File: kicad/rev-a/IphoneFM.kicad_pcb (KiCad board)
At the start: 2 copper layers, 0 parts

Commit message: Step 3.4: board outline at the sketch's coordinates, origins on its top-left corner
Co-Authored-By: Claude Opus 5.5 <noreply@anthropic.com>
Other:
- board outline added: 46.5 x 71.4 mm
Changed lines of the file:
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@@
 		(capping no)
 		(filling no)
+		(aux_axis_origin 12.7 59.56)
+		(grid_origin 12.7 59.56)
 		(pcbplotparams
 			(layerselection 0x00000000_00000000_55555555_5755f5ff)
@@
 		)
 	)
+	(gr_rect
+		(start 12.7 59.56)
+		(end 59.15 130.96)
+		(stroke
+			(width 0.05)
+			(type solid)
+		)
+		(fill no)
+		(layer "Edge.Cuts")
+	)
 	(embedded_fonts no)

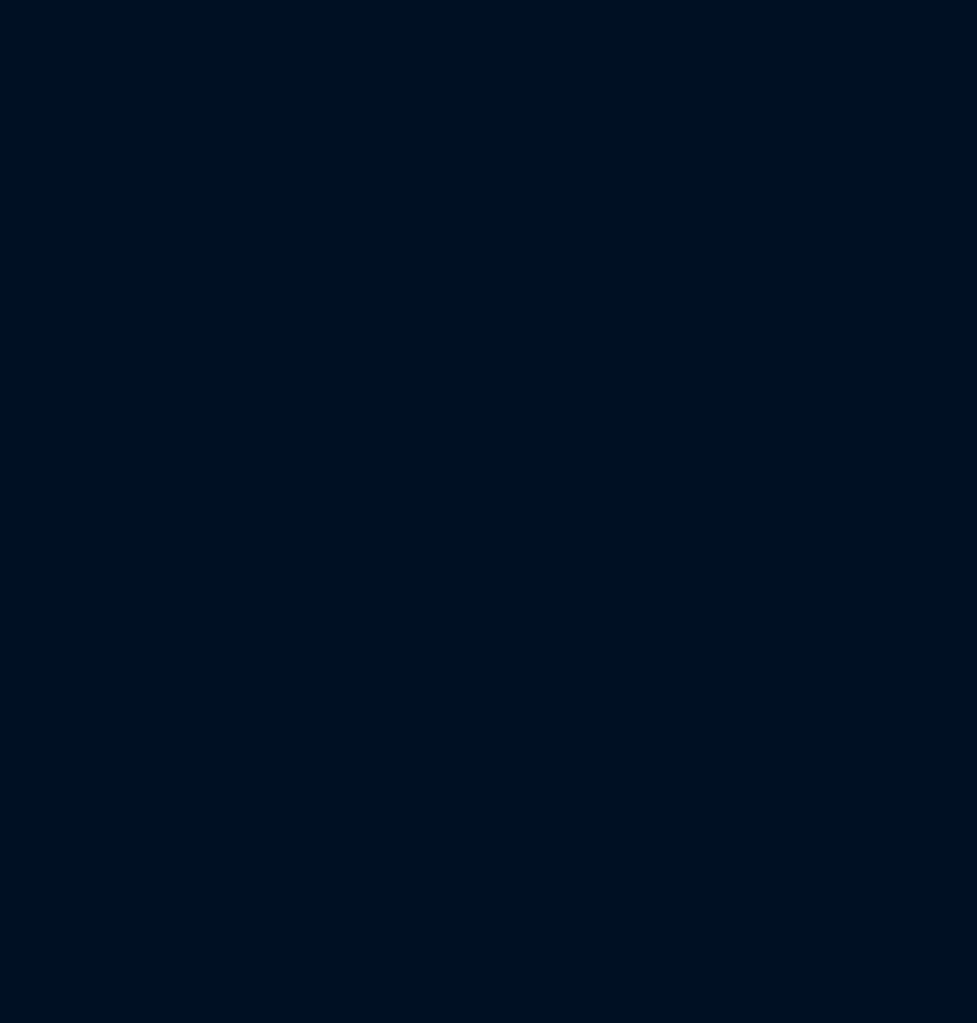
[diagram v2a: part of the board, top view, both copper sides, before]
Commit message: Step 4.1: parts brought across from the schematic (106 footprints), rules restored after KiCad's stale save, mask material named so KiCad keeps its Dk
Co-Authored-By: Claude Opus 5.5 <noreply@anthropic.com>
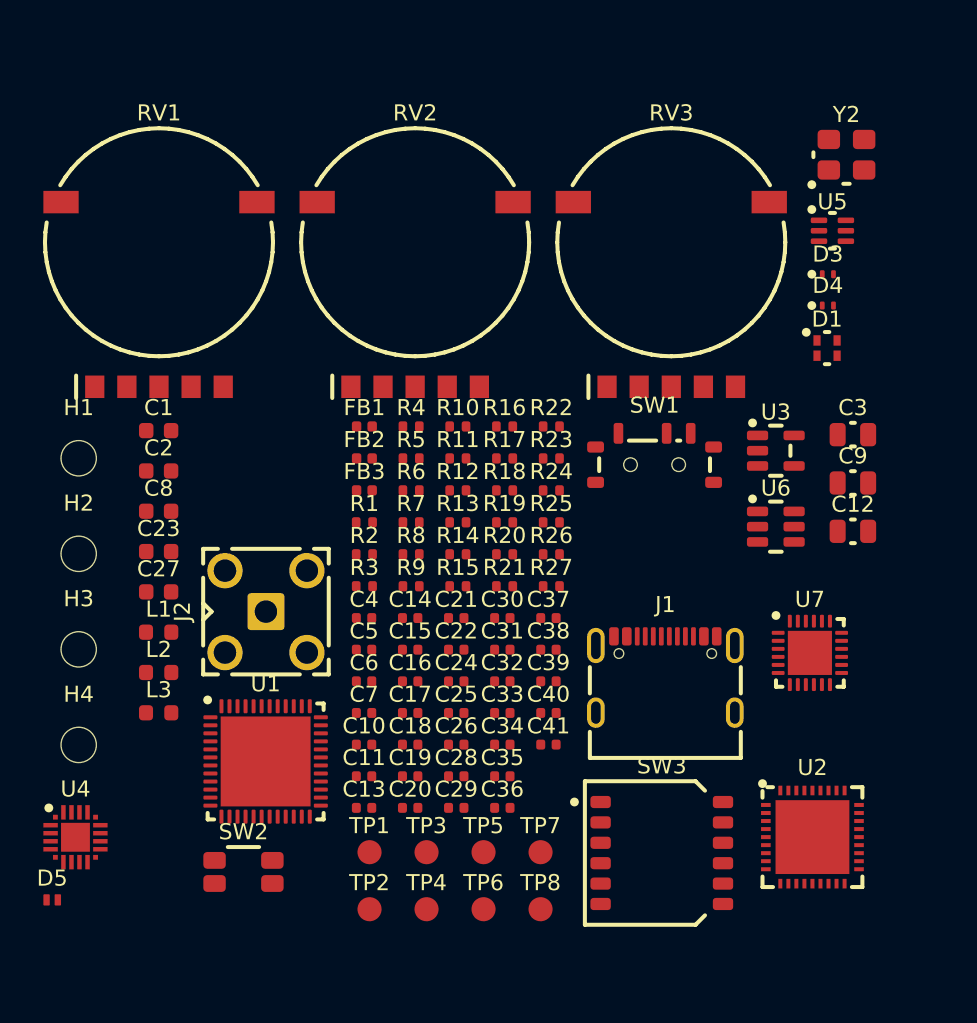
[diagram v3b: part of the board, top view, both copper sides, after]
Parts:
- added C1: 1 µF X7R 16 V, IphoneFM:C_0603_1608Metric, F.Cu at (-45.8, 85.1)
- added C10: 100 nF X7R 16 V, IphoneFM:C_0402_1005Metric, F.Cu at (-33.1, 104.6)
- added C11: 100 nF X7R 16 V, IphoneFM:C_0402_1005Metric, F.Cu at (-33.1, 106.6)
- added C12: 10 µF X5R 16 V, IphoneFM:C_0805_2012Metric, F.Cu at (-2.62, 91.3)
- added C13: 100 nF X7R 16 V, IphoneFM:C_0402_1005Metric, F.Cu at (-33.1, 108.6)
- added C14: 100 nF X7R 16 V, IphoneFM:C_0402_1005Metric, F.Cu at (-30.2, 96.7)
- added C15: 100 nF X7R 16 V, IphoneFM:C_0402_1005Metric, F.Cu at (-30.2, 98.7)
- added C16: 100 nF X7R 16 V, IphoneFM:C_0402_1005Metric, F.Cu at (-30.2, 100.7)
- added C17: 100 nF X7R 16 V, IphoneFM:C_0402_1005Metric, F.Cu at (-30.2, 102.6)
- added C18: 100 nF X7R 16 V, IphoneFM:C_0402_1005Metric, F.Cu at (-30.2, 104.6)
- added C19: 100 nF X7R 16 V, IphoneFM:C_0402_1005Metric, F.Cu at (-30.2, 106.6)
- added C2: 1 µF X7R 16 V, IphoneFM:C_0603_1608Metric, F.Cu at (-45.8, 87.6)
- added C20: 100 nF X7R 16 V, IphoneFM:C_0402_1005Metric, F.Cu at (-30.2, 108.6)
- added C21: 100 nF X7R 16 V, IphoneFM:C_0402_1005Metric, F.Cu at (-27.3, 96.7)
- added C22: 100 nF X7R 16 V, IphoneFM:C_0402_1005Metric, F.Cu at (-27.3, 98.7)
- added C23: 2.2 µF X5R 16 V, IphoneFM:C_0603_1608Metric, F.Cu at (-45.8, 92.6)
- added C24: 100 pF C0G, IphoneFM:C_0402_1005Metric, F.Cu at (-27.3, 100.7)
- added C25: 1.5 nF C0G, IphoneFM:C_0402_1005Metric, F.Cu at (-27.3, 102.6)
- added C26: 100 pF C0G, IphoneFM:C_0402_1005Metric, F.Cu at (-27.3, 104.6)
- added C27: 1 µF X7R 16 V, IphoneFM:C_0603_1608Metric, F.Cu at (-45.8, 95.1)
- added C28: 33 pF C0G, IphoneFM:C_0402_1005Metric, F.Cu at (-27.3, 106.6)
- added C29: 56 pF C0G, IphoneFM:C_0402_1005Metric, F.Cu at (-27.3, 108.6)
- added C3: 10 µF X5R 16 V, IphoneFM:C_0805_2012Metric, F.Cu at (-2.62, 85.3)
- added C30: 33 pF C0G, IphoneFM:C_0402_1005Metric, F.Cu at (-24.4, 96.7)
- added C31: 1 nF C0G, IphoneFM:C_0402_1005Metric, F.Cu at (-24.4, 98.7)
- added C32: 22 nF X7R 50 V, IphoneFM:C_0402_1005Metric, F.Cu at (-24.4, 100.7)
- added C33: 100 nF X7R 16 V, IphoneFM:C_0402_1005Metric, F.Cu at (-24.4, 102.6)
- added C34: 1 nF C0G, IphoneFM:C_0402_1005Metric, F.Cu at (-24.4, 104.6)
- added C35: 6 pF C0G, IphoneFM:C_0402_1005Metric, F.Cu at (-24.4, 106.6)
- added C36: 3.3 pF C0G, IphoneFM:C_0402_1005Metric, F.Cu at (-24.4, 108.6)
- added C37: 33 pF C0G, IphoneFM:C_0402_1005Metric, F.Cu at (-21.6, 96.7)
- added C38: 33 pF C0G, IphoneFM:C_0402_1005Metric, F.Cu at (-21.6, 98.7)
- added C39: 100 nF X7R 16 V, IphoneFM:C_0402_1005Metric, F.Cu at (-21.6, 100.7)
- added C4: 100 nF X7R 16 V, IphoneFM:C_0402_1005Metric, F.Cu at (-33.1, 96.7)
- added C40: 100 nF X7R 16 V, IphoneFM:C_0402_1005Metric, F.Cu at (-21.6, 102.6)
- added C41: 100 nF X7R 16 V, IphoneFM:C_0402_1005Metric, F.Cu at (-21.6, 104.6)
- added C5: 100 nF X7R 16 V, IphoneFM:C_0402_1005Metric, F.Cu at (-33.1, 98.7)
- added C6: 100 nF X7R 16 V, IphoneFM:C_0402_1005Metric, F.Cu at (-33.1, 100.7)
- added C7: 100 nF X7R 16 V, IphoneFM:C_0402_1005Metric, F.Cu at (-33.1, 102.6)
- added C8: 1 µF X7R 16 V, IphoneFM:C_0603_1608Metric, F.Cu at (-45.8, 90.1)
- added C9: 4.7 µF X7R 16 V, IphoneFM:C_0805_2012Metric, F.Cu at (-2.62, 88.3)
- added D1: RGB LED, common anode, IphoneFM:LED_RGB_XINGLIGHT_XL-1615RGBC_1.6x1.5mm, F.Cu at (-4.22, 79.9)
- added D3: ESD 5.5 V, IphoneFM:Texas_DPY0002A_0.6x1mm_P0.65mm, F.Cu at (-4.17, 75.3)
- added D4: ESD 5.5 V, IphoneFM:Texas_DPY0002A_0.6x1mm_P0.65mm, F.Cu at (-4.17, 77.3)
- added D5: ESD 5 V, 0.5 pF, IphoneFM:D_SOD-882, F.Cu at (-52.5, 114.3)
- added FB1: 75 Ω at 100 MHz, IphoneFM:L_0402_1005Metric, F.Cu at (-33.0, 84.8)
- added FB2: 600 Ω at 100 MHz, IphoneFM:L_0402_1005Metric, F.Cu at (-33.0, 86.8)
- added FB3: 600 Ω at 100 MHz, IphoneFM:L_0402_1005Metric, F.Cu at (-33.0, 88.8)
- added H1: M2, IphoneFM:MountingHole_2.2mm_M2, F.Cu at (-50.8, 86.8)
- added H2: M2, IphoneFM:MountingHole_2.2mm_M2, F.Cu at (-50.8, 92.7)
- added H3: M2, IphoneFM:MountingHole_2.2mm_M2, F.Cu at (-50.8, 98.7)
- added H4: M2, IphoneFM:MountingHole_2.2mm_M2, F.Cu at (-50.8, 104.6)
- added J1: USB 2.0 Type-C, IphoneFM:USB_C_Receptacle_HRO_TYPE-C-31-M-12_2020, F.Cu at (-14.3, 101.5)
- added J2: SMA jack, IphoneFM:SMA_BAT_Wireless_BWSMA-KWE-Z001, F.Cu at (-39.2, 96.3)
- added L1: 150 nH 2%, IphoneFM:L_0603_1608Metric, F.Cu at (-45.8, 97.6)
- added L2: 100 nH 2%, IphoneFM:L_0603_1608Metric, F.Cu at (-45.8, 100.1)
- added L3: 100 nH 2%, IphoneFM:L_0603_1608Metric, F.Cu at (-45.8, 102.6)
- added R1: 5.1 kΩ 1%, IphoneFM:R_0402_1005Metric, F.Cu at (-33.0, 90.8)
- added R10: 10 kΩ 1%, IphoneFM:R_0402_1005Metric, F.Cu at (-27.2, 84.8)
- added R11: 10 kΩ 1%, IphoneFM:R_0402_1005Metric, F.Cu at (-27.2, 86.8)
- added R12: 10 kΩ 1%, IphoneFM:R_0402_1005Metric, F.Cu at (-27.2, 88.8)
- added R13: 10 kΩ 1%, IphoneFM:R_0402_1005Metric, F.Cu at (-27.2, 90.8)
- added R14: 10 kΩ 1%, IphoneFM:R_0402_1005Metric, F.Cu at (-27.2, 92.8)
- added R15: 10 kΩ 1%, IphoneFM:R_0402_1005Metric, F.Cu at (-27.2, 94.8)
- added R16: 1 kΩ 1%, IphoneFM:R_0402_1005Metric, F.Cu at (-24.3, 84.8)
- added R17: 1 kΩ 1%, IphoneFM:R_0402_1005Metric, F.Cu at (-24.3, 86.8)
- added R18: 100 kΩ 1%, IphoneFM:R_0402_1005Metric, F.Cu at (-24.3, 88.8)
- added R19: 10 kΩ 1%, IphoneFM:R_0402_1005Metric, F.Cu at (-24.3, 90.8)
- added R2: 5.1 kΩ 1%, IphoneFM:R_0402_1005Metric, F.Cu at (-33.0, 92.8)
- added R20: 6.8 kΩ 1%, IphoneFM:R_0402_1005Metric, F.Cu at (-24.3, 92.8)
- added R21: 6.8 kΩ 1%, IphoneFM:R_0402_1005Metric, F.Cu at (-24.3, 94.8)
- added R22: 604 Ω 1%, IphoneFM:R_0402_1005Metric, F.Cu at (-21.4, 84.8)
- added R23: 2 kΩ 1%, IphoneFM:R_0402_1005Metric, F.Cu at (-21.4, 86.8)
- added R24: 2 kΩ 1%, IphoneFM:R_0402_1005Metric, F.Cu at (-21.4, 88.8)
- added R25: 510 Ω 1%, IphoneFM:R_0402_1005Metric, F.Cu at (-21.4, 90.8)
- added R26: 390 Ω 1%, IphoneFM:R_0402_1005Metric, F.Cu at (-21.4, 92.8)
- added R27: 390 Ω 1%, IphoneFM:R_0402_1005Metric, F.Cu at (-21.4, 94.8)
- added R3: 10 kΩ 1%, IphoneFM:R_0402_1005Metric, F.Cu at (-33.0, 94.8)
- added R4: 33 Ω 1%, IphoneFM:R_0402_1005Metric, F.Cu at (-30.1, 84.8)
- added R5: 1.1 kΩ 1%, IphoneFM:R_0402_1005Metric, F.Cu at (-30.1, 86.8)
- added R6: 33 Ω 1%, IphoneFM:R_0402_1005Metric, F.Cu at (-30.1, 88.8)
- added R7: 33 Ω 1%, IphoneFM:R_0402_1005Metric, F.Cu at (-30.1, 90.8)
- added R8: 33 Ω 1%, IphoneFM:R_0402_1005Metric, F.Cu at (-30.1, 92.8)
- added R9: 10 kΩ 1%, IphoneFM:R_0402_1005Metric, F.Cu at (-30.1, 94.8)
- added RV1: 10 kΩ 3B, IphoneFM:Potentiometer_Alps_RK10J_Reflow_Thumbwheel_14mm, F.Cu at (-45.8, 73.3)
- added RV2: 10 kΩ 3B, IphoneFM:Potentiometer_Alps_RK10J_Reflow_Thumbwheel_14mm, F.Cu at (-29.9, 73.3)
- added RV3: 10 kΩ 3B, IphoneFM:Potentiometer_Alps_RK10J_Reflow_Thumbwheel_14mm, F.Cu at (-13.9, 73.3)
- added SW1: SPDT, IphoneFM:SW_SPDT_Shouhan_MSK12C02_Tabs4, F.Cu at (-15.0, 87.2)
- added SW2: SPST, IphoneFM:SW_SPST_EVQP7A, F.Cu at (-40.6, 112.5)
- added SW3: 6 × SPST, IphoneFM:SW_DIP_SPSTx06_Side_CK_TDP06H1SBD1_W7.62mm_P1.27mm, F.Cu at (-14.5, 111.4)
- added TP1: VBUS, IphoneFM:TestPoint_Pad_D1.5mm, F.Cu at (-32.7, 111.3)
- added TP2: 3V3, IphoneFM:TestPoint_Pad_D1.5mm, F.Cu at (-32.7, 114.9)
- added TP3: GND, IphoneFM:TestPoint_Pad_D1.5mm, F.Cu at (-29.2, 111.3)
- added TP4: RF_MODE, IphoneFM:TestPoint_Pad_D1.5mm, F.Cu at (-29.2, 114.9)
- added TP5: LMX_MUX, IphoneFM:TestPoint_Pad_D1.5mm, F.Cu at (-25.6, 111.3)
- added TP6: NRST, IphoneFM:TestPoint_Pad_D1.5mm, F.Cu at (-25.6, 114.9)
- added TP7: SWCLK, IphoneFM:TestPoint_Pad_D1.5mm, F.Cu at (-22.1, 111.3)
- added TP8: SWDIO, IphoneFM:TestPoint_Pad_D1.5mm, F.Cu at (-22.1, 114.9)
- added U1: MCU, IphoneFM:QFN-48-1EP_7x7mm_P0.5mm_EP5.6x5.6mm, F.Cu at (-39.2, 105.7)
- added U2: Synthesizer, IphoneFM:TI_NJK0036A_WQFN-36-1EP_6x6mm_P0.5mm_EP4.6x4.6mm, F.Cu at (-5.13, 110.4)
- added U3: 3.3 V 600 mA LDO, IphoneFM:SOT-23-5, F.Cu at (-7.42, 86.3)
- added U4: FM receiver, IphoneFM:SiliconLabs_QFN-20-1EP_3x3mm_P0.5mm_EP1.8x1.8mm, F.Cu at (-51.0, 110.4)
- added U5: SPDT RF switch, IphoneFM:SOT-363_SC-70-6, F.Cu at (-3.89, 72.6)
- added U6: USB ESD array, IphoneFM:SOT-23-6, F.Cu at (-7.42, 91.0)
- added U7: Digital step attenuator, IphoneFM:QFN-24-1EP_4x4mm_P0.5mm_EP2.75x2.75mm, F.Cu at (-5.29, 98.9)
- added Y2: 20 MHz CMOS XO, IphoneFM:Oscillator_SMD_SiT_PQFN-4Pin_3.2x2.5mm, F.Cu at (-3.02, 67.9)

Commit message: Step 4.2: board saved with the parts grouped beside it; ticked, approved by the user
Co-Authored-By: Claude Opus 5.5 <noreply@anthropic.com>
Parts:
- moved D5 147.6 mm to (91.9, 145.2)
- moved L3 136.7 mm to (86.6, 136.3)
- moved C23 134.4 mm to (85.6, 64.4)
- moved C27 134.2 mm to (87.5, 80.7)
- moved L2 133.9 mm to (83.0, 136.3)
- moved C6 132.1 mm to (98.9, 96.2)
- moved R3 132.0 mm to (98.9, 93.7)
- moved C25 130.2 mm to (95.7, 60.0)
- moved R16 130.2 mm to (92.0, 143.3)
- moved C19 130.2 mm to (92.2, 62.1)
- moved C8 129.4 mm to (83.5, 93.9)
- moved C16 128.9 mm to (92.2, 60.0)
- moved C18 128.9 mm to (92.2, 64.1)
- moved C5 128.0 mm to (94.9, 98.8)
- moved R17 127.8 mm to (92.0, 139.7)
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
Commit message: Step 4.3: board saved with J1 placed and locked; ticked, approved by the user
Co-Authored-By: Claude Opus 5.5 <noreply@anthropic.com>
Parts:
- moved J1 38.5 mm to (35.9, 127.8)
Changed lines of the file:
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@@
 	)
 	(footprint "IphoneFM:USB_C_Receptacle_HRO_TYPE-C-31-M-12_2020"
+		(locked yes)
 		(layer "F.Cu")
-		(at 74.47 127.45)
+		(at 35.925 127.77)
 		(descr "USB Type-C receptacle for USB 2.0 and PD, HRO TYPE-C-31-M-12; pads and holes per HRO's recommended PCB layout, drawing dated 2020-12-08 (KiCad's footprint follows the 2015 drawing)")
 		(tags "usb usb-c 2.0 pd")
@@
 		)
 		(embedded_fonts no)
-		(model "${KICAD10_3DMODEL_DIR}/Connector_USB.3dshapes/USB_C_Receptacle_HRO_TYPE-C-31-M-12.step"
-			(offset
-				(xyz 0 0 0)
-			)
-			(scale
-				(xyz 1 1 1)
-			)
-			(rotate
-				(xyz 0 0 0)
-			)
-		)
 	)
 	(footprint "IphoneFM:Texas_DPY0002A_0.6x1mm_P0.65mm"

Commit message: Step 4.4: board saved with J2 placed and locked; ticked, approved by the user
Co-Authored-By: Claude Opus 5.5 <noreply@anthropic.com>
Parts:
- moved J2 30.1 mm to (55.0, 126.8), turned to -90 degrees

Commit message: Step 4.5: board saved with the wheels placed and locked; ticked, approved by the user
Co-Authored-By: Claude Opus 5.5 <noreply@anthropic.com>
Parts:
- moved RV1 78.0 mm to (17.8, 78.0), turned to 90 degrees
- moved RV2 67.8 mm to (17.8, 95.0), turned to 90 degrees
- moved RV3 64.6 mm to (17.8, 112.0), turned to 90 degrees

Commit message: Step 4.6: board saved with the switches placed and locked; ticked, approved by the user
Co-Authored-By: Claude Opus 5.5 <noreply@anthropic.com>
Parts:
- moved SW2 75.8 mm to (25.5, 129.2)
- moved SW1 70.1 mm to (14.7, 125.5), turned to -90 degrees
- moved SW3 49.1 mm to (35.9, 64.5), turned to -90 degrees
